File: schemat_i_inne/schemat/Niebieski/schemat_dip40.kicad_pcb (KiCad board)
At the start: 2 copper layers, 260.4 x 151.1 mm, 22 parts, among them J1 Hole1, J2 Hole2, J3 Hole3, J4 Hole4, SW1 SW_DIP_x01, SW2 Left, SW3 Up, SW4 Down, SW5 Right, SW6 Jump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

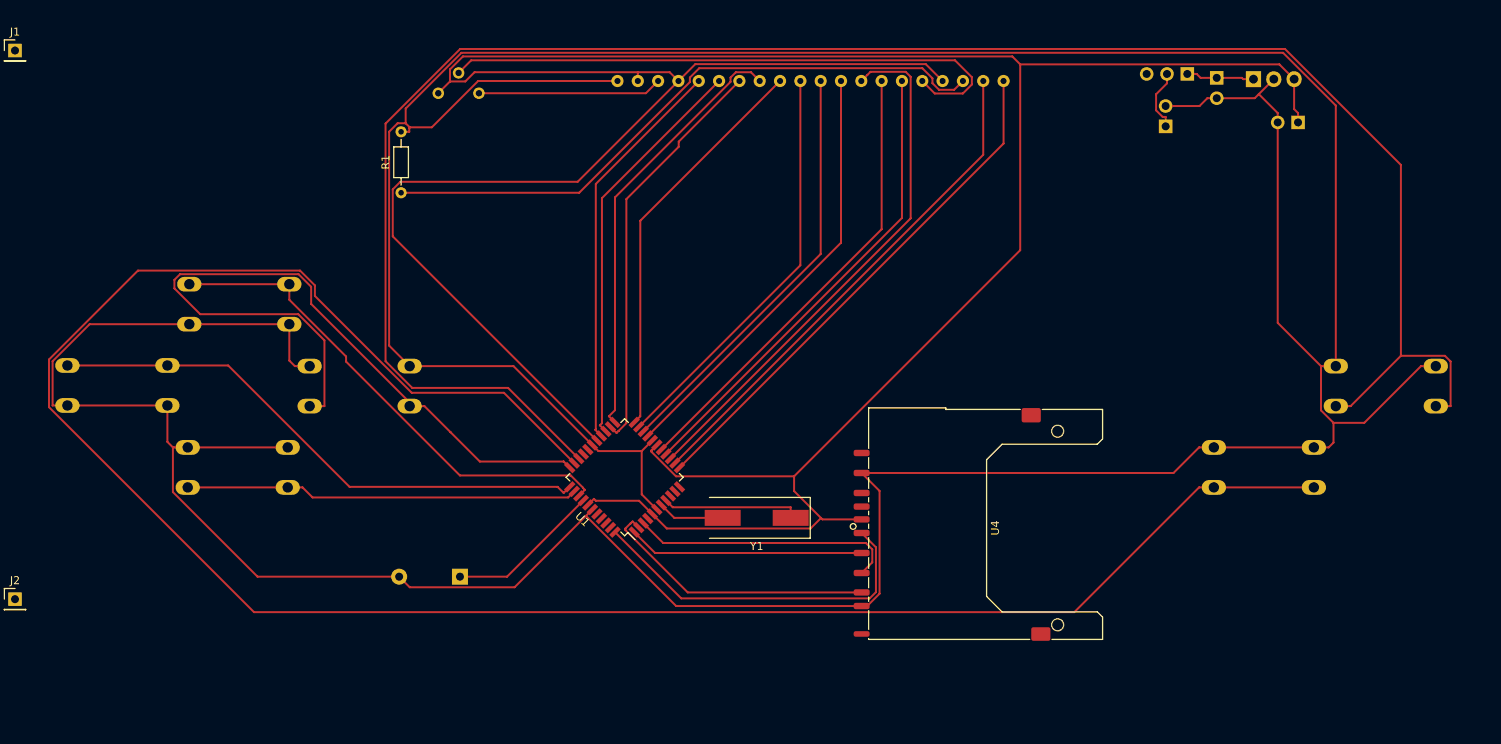
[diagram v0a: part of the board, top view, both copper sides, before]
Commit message: Wszystkie polaczenia
Zrealizowano wszystkie polaczenia, wygaldaja okropnie ale sa XD
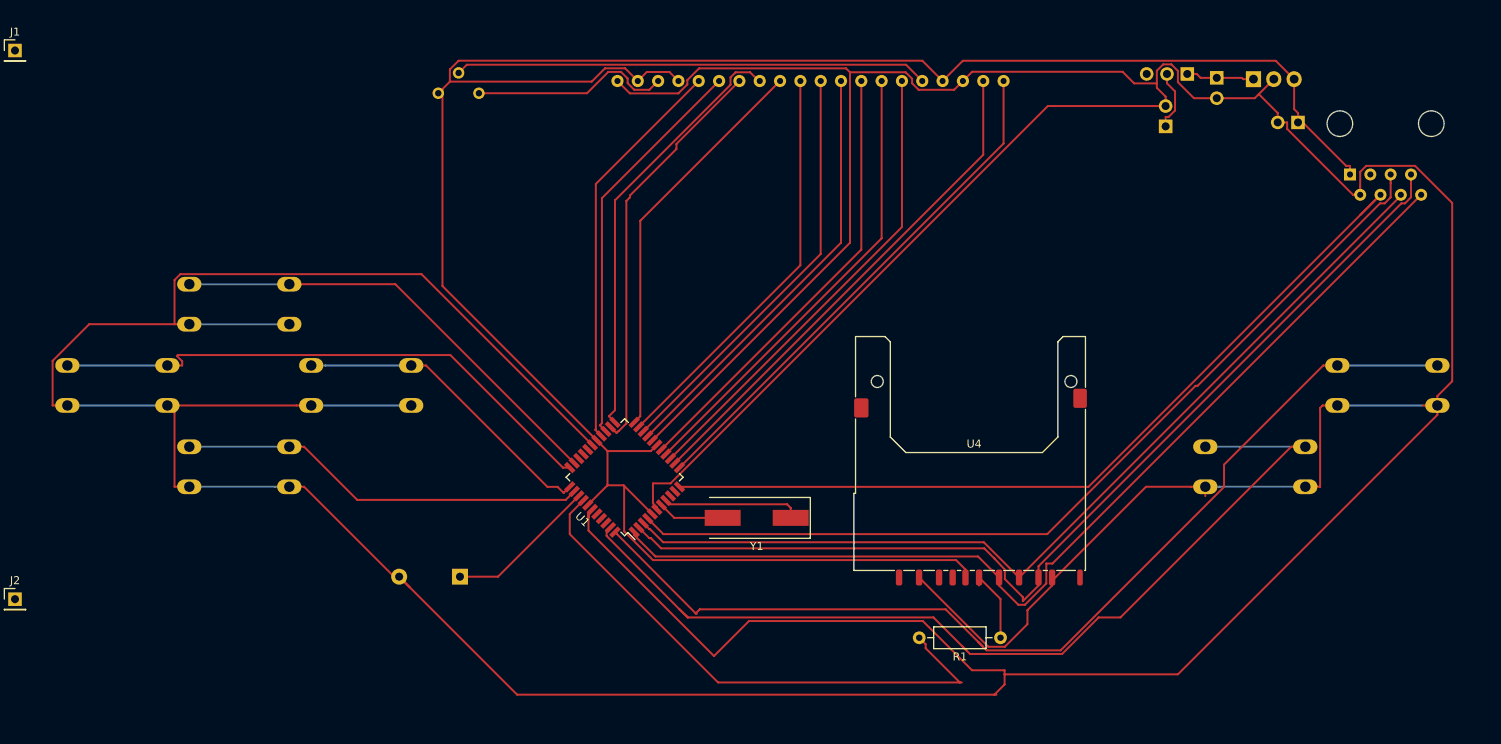
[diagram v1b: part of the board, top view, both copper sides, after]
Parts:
- added J5: RJ45, Connector_RJ:RJ45_Amphenol_54602-x08_Horizontal, B.Cu at (211.3, 72.6)
- R1: footprint Resistor_THT:R_Axial_DIN0204_L3.6mm_D1.6mm_P7.62mm_Horizontal -> Resistor_THT:R_Axial_DIN0207_L6.3mm_D2.5mm_P10.16mm_Horizontal
- moved R1 93.3 mm to (167.6, 130.6), turned to 180 degrees
- moved SW5 13.7 mm to (94.0, 96.5), turned to 180 degrees
- moved SW4 13.7 mm to (78.7, 106.7), turned to 180 degrees
- moved SW7 13.7 mm to (222.2, 96.5), turned to 180 degrees
- moved SW6 12.5 mm to (205.7, 106.7), turned to 180 degrees
- moved U4 6.93 mm to (164.3, 115.8), turned to 0 degrees
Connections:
- R1 pad 2: GND -> Net-(R1-Pad2)
- U1 pad 31: Net-(SW7-Pad1) -> Net-(U1-Pad31)
- U1 pad 32: Net-(SW6-Pad1) -> Net-(SW3-Pad1)
- U1 pad 33: Net-(SW5-Pad1) -> Net-(SW2-Pad1)
- U1 pad 34: Net-(SW2-Pad1) -> Net-(SW5-Pad1)
- U1 pad 36: Net-(SW3-Pad1) -> Net-(BZ1-Pad1)
- U1 pad 37: Net-(BZ1-Pad1) -> Net-(R1-Pad2)
- U1 pad 43: Net-(U1-Pad43) -> Net-(SW6-Pad1)
- U1 pad 44: Net-(U1-Pad44) -> Net-(SW7-Pad1)
- U3 pad 3: Net-(R1-Pad1) -> GND
- U3 pad 6: Net-(U1-Pad15) -> Net-(U1-Pad14)
- U3 pad 7: Net-(U1-Pad16) -> Net-(U1-Pad15)
- U3 pad 8: Net-(U1-Pad14) -> Net-(U1-Pad16)
- U4 pad 4: Net-(U1-Pad44) -> Net-(R1-Pad1)
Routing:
- net GND: track 607.3 -> 805.6 mm
- net Net-(SW6-Pad1): track 262.1 -> 120.2 mm
- net Net-(SW7-Pad1): track 244.2 -> 126.8 mm
- net Net-(J5-Pad5): track 0.00 -> 114.0 mm
- net VCC: track 391.9 -> 285.4 mm
- net Net-(J5-Pad4): track 0.00 -> 106.3 mm
- net Net-(J5-Pad8): track 29.5 -> 125.9 mm
- net Net-(J5-Pad7): track 35.3 -> 126.8 mm
- net Net-(J5-Pad6): track 33.5 -> 117.4 mm
- net Net-(R1-Pad2): track 0.00 -> 69.3 mm
- net Net-(R1-Pad1): track 78.9 -> 9.64 mm
- net Net-(SW5-Pad1): track 94.0 -> 39.2 mm
- net Net-(U1-Pad44): track 44.5 -> 0.00 mm
- net Net-(RV1-Pad2): track 73.9 -> 59.2 mm
- net Net-(U1-Pad14): track 67.1 -> 59.2 mm
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
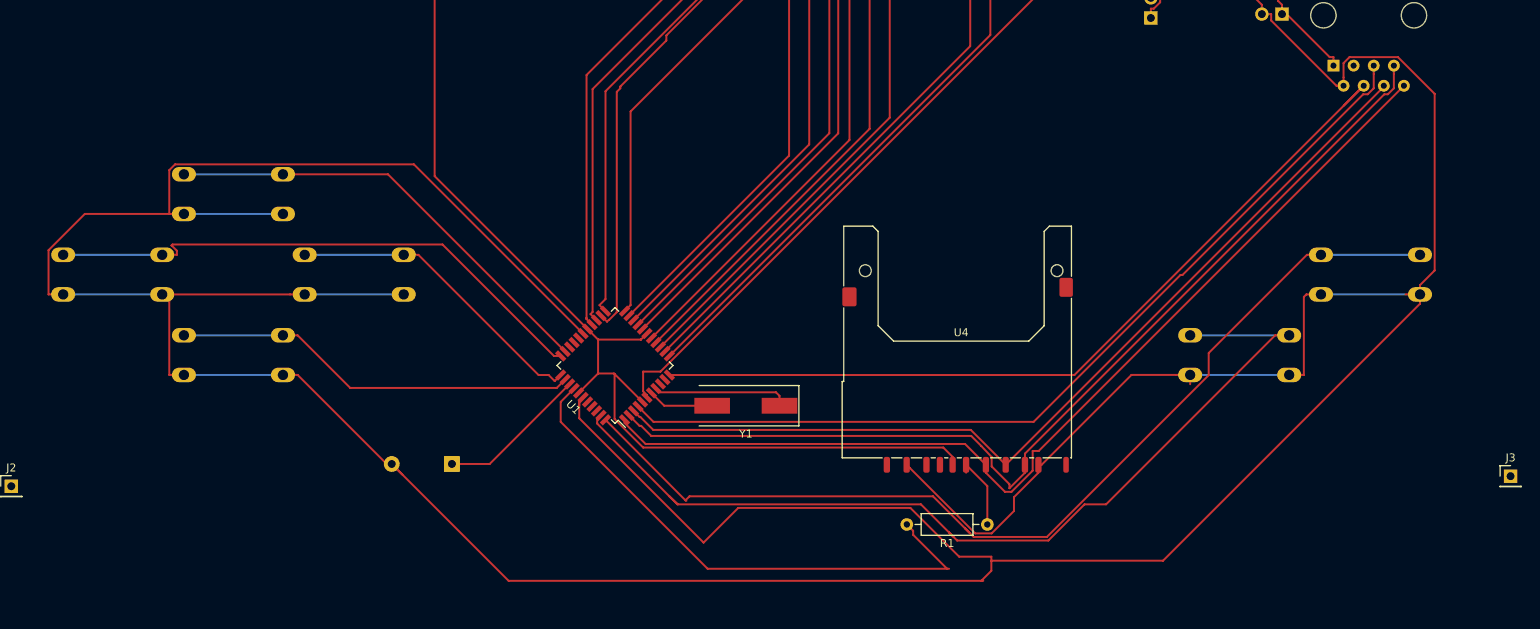
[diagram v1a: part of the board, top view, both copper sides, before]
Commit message: Awful, but should work XD
Strasznie brzydko, wszystkie sciezki do poprawy graficznej.
Zamieniono przyciski tak aby były w dobrych miejscach
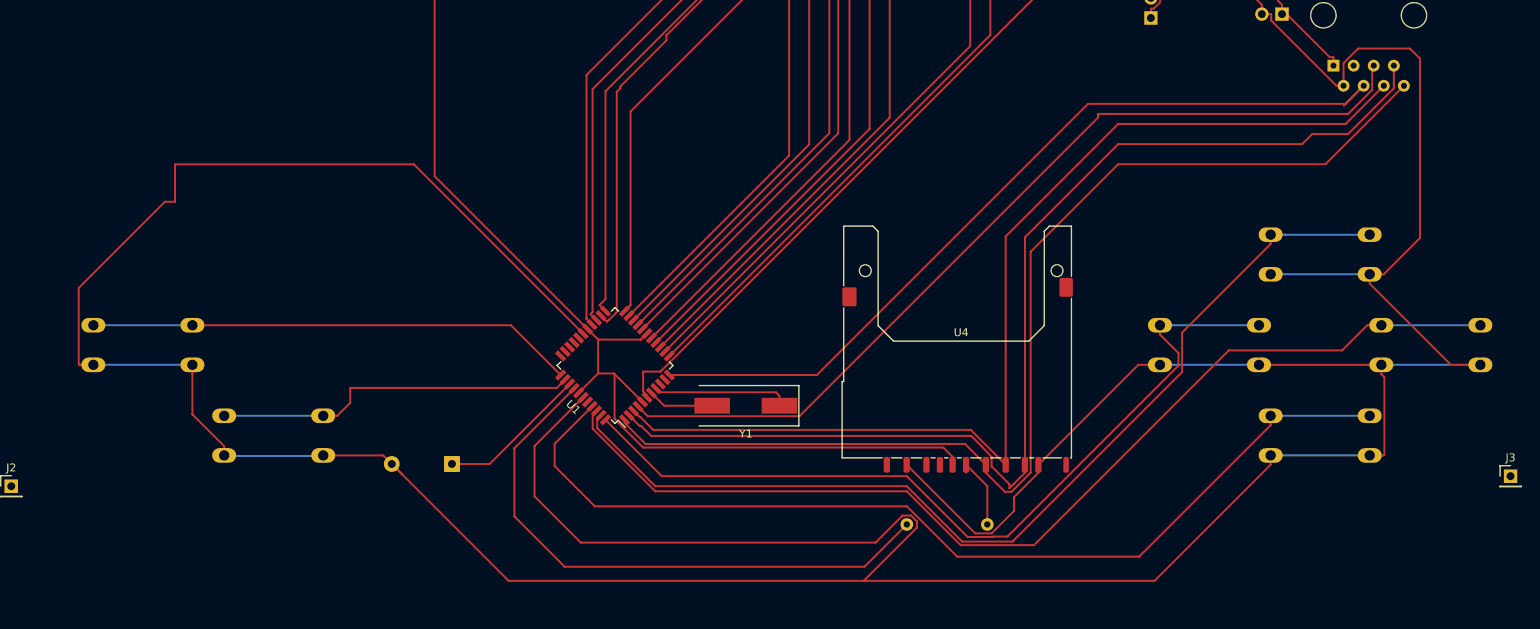
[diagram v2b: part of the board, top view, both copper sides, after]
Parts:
- R1: moved to B.Cu
- moved SW7 155.2 mm to (67.3, 105.4)
- moved SW2 138.7 mm to (201.9, 105.4)
- moved SW4 137.5 mm to (215.9, 116.8)
- moved SW3 137.4 mm to (215.9, 94.0)
- moved SW5 136.2 mm to (229.9, 105.4)
- moved SW6 122.3 mm to (83.8, 116.8)
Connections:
- U1 pad 32: Net-(SW3-Pad1) -> Net-(U1-Pad32)
- U1 pad 33: Net-(SW2-Pad1) -> Net-(U1-Pad33)
- U1 pad 34: Net-(SW5-Pad1) -> Net-(SW7-Pad1)
- U1 pad 35: Net-(SW4-Pad1) -> Net-(SW6-Pad1)
- U1 pad 41: Net-(U1-Pad41) -> Net-(SW4-Pad1)
- U1 pad 42: Net-(U1-Pad42) -> Net-(SW5-Pad1)
- U1 pad 43: Net-(SW6-Pad1) -> Net-(SW3-Pad1)
- U1 pad 44: Net-(SW7-Pad1) -> Net-(SW2-Pad1)
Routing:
- net Net-(SW5-Pad1): track 39.2 -> 132.1 mm
- net Net-(SW6-Pad1): track 120.2 -> 46.0 mm
- net Net-(SW4-Pad1): track 51.3 -> 125.2 mm
- net Net-(SW3-Pad1): track 57.4 -> 124.9 mm
- net Net-(SW7-Pad1): track 126.8 -> 61.6 mm
- net Net-(SW2-Pad1): track 70.8 -> 106.0 mm
- net Net-(J5-Pad6): track 117.4 -> 134.2 mm
- net Net-(J5-Pad7): track 126.8 -> 142.8 mm
- net Net-(J5-Pad8): track 125.9 -> 140.8 mm
- net GND: track 805.6 -> 792.9 mm
- net Net-(R1-Pad2): track 69.3 -> 74.3 mm

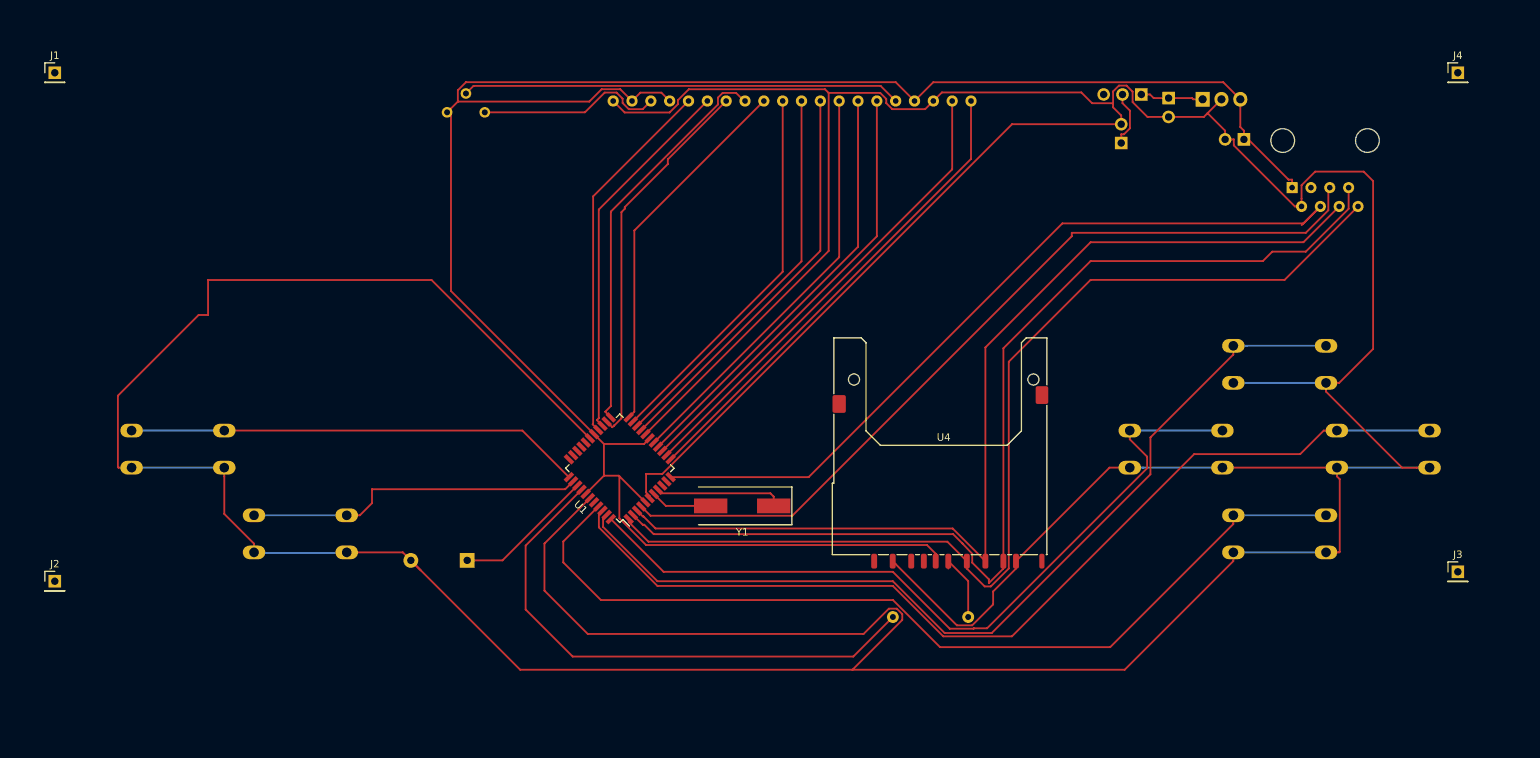
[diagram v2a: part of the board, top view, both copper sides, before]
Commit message: Strefy i poprawki
Dodano strefe GND i poprawiono juz czesc sciezek
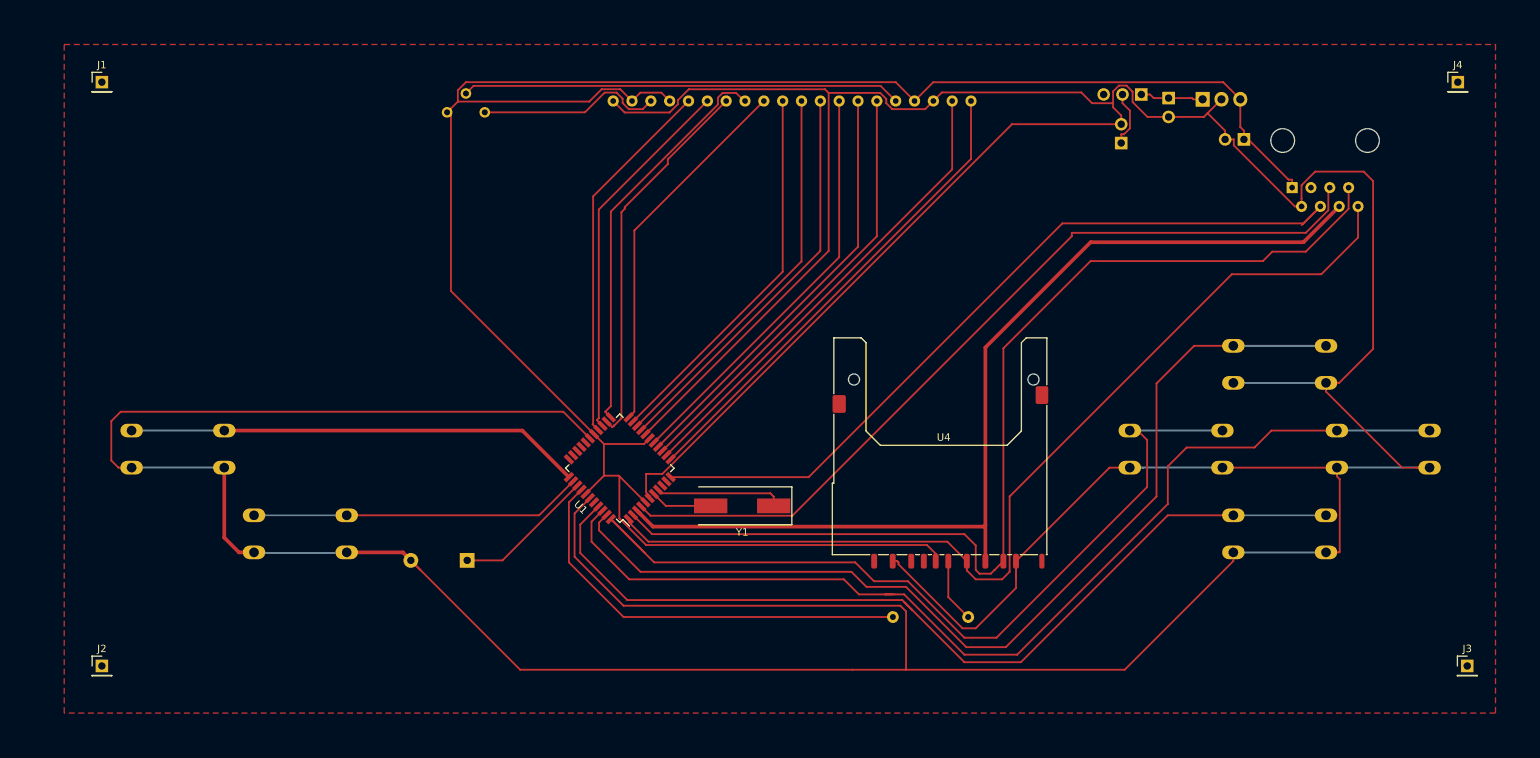
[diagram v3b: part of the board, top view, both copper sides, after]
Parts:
- moved J2 13.1 mm to (50.8, 137.2)
- moved J3 12.8 mm to (234.9, 137.2)
- moved J1 6.48 mm to (50.8, 58.4)
- moved J4 1.27 mm to (233.7, 58.4)
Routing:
- net GND: track 792.9 -> 766.1 mm
- net Net-(R1-Pad2): track 74.3 -> 57.9 mm
- net Net-(SW2-Pad1): track 106.0 -> 115.5 mm
- net Net-(J5-Pad8): track 140.8 -> 132.2 mm
- net Net-(SW5-Pad1): track 132.1 -> 140.6 mm
- net Net-(SW3-Pad1): track 124.9 -> 132.8 mm
- net Net-(J5-Pad6): track 134.2 -> 132.4 mm
- net Net-(SW4-Pad1): track 125.2 -> 123.6 mm
- net Net-(SW6-Pad1): track 46.0 -> 44.9 mm
- net Net-(R1-Pad1): track 9.64 -> 8.64 mm
- net Net-(J5-Pad7): track 142.8 -> 142.1 mm
- added copper zone on F.Cu, net GND
